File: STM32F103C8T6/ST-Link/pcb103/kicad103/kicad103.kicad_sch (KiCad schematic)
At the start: 32 parts, among them IC1 LD1117DT33TR, J1 0480372200, J2 Conn_01x02_Socket, J3 Conn_02x05_Odd_Even, J5 Conn_01x16_Pin, J7 Conn_01x04_Pin, J8 Conn_01x05_Socket, J9 Conn_01x17_Pin, U1 STM32F103C8T6, Y1 8MHz 20pF

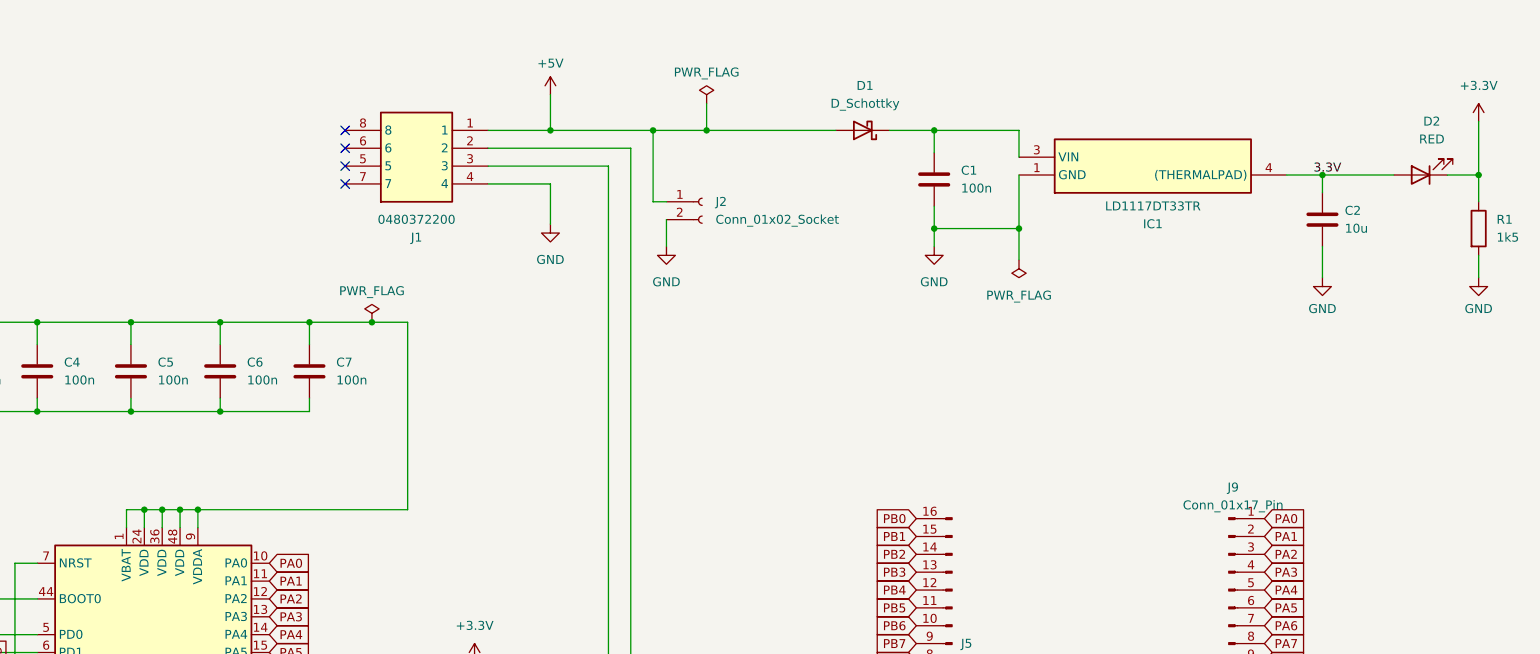
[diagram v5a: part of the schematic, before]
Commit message: Fix power lines
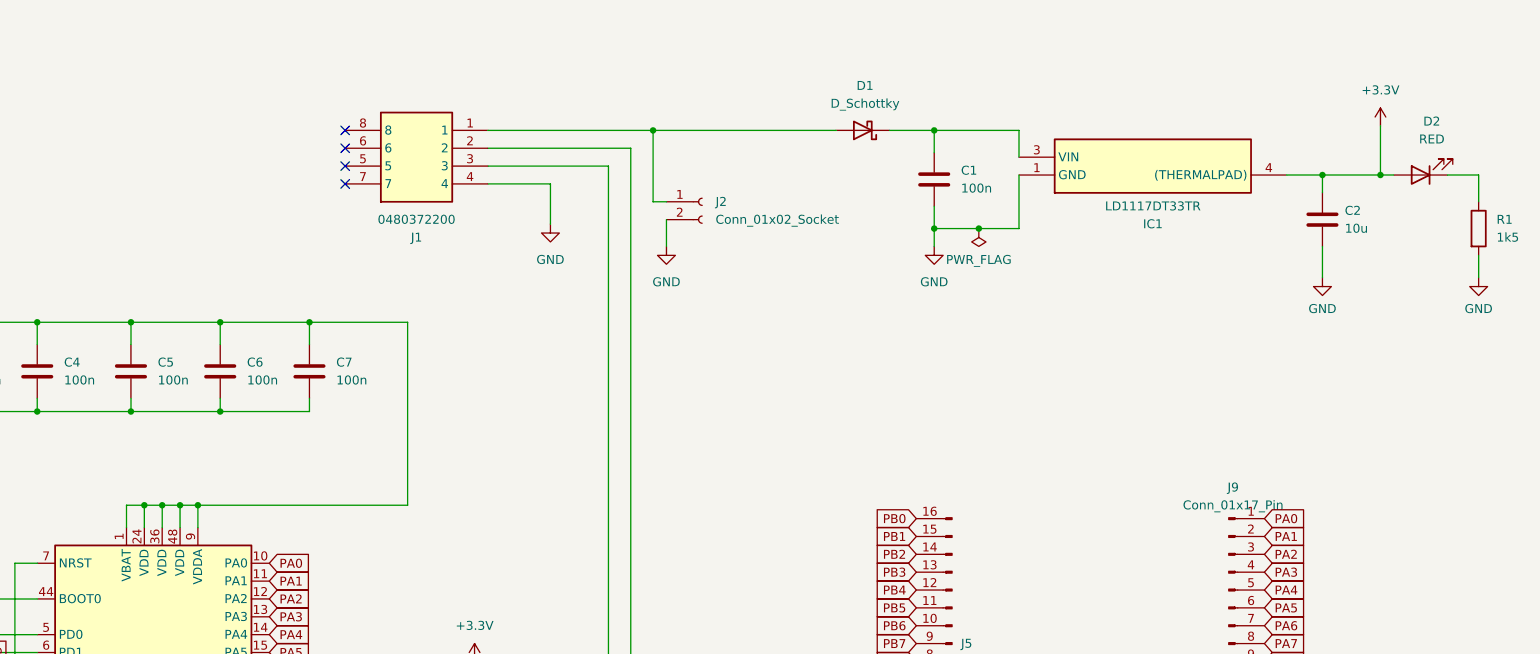
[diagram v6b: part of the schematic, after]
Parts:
- IC1: footprint Library:TO228P972X240-3N -> TO228P972X240-3N
- J1: footprint Library:0480372200 -> 0480372200
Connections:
- net 3.3V is gone; now on net +3.3V: C2.1, D2.2 (A), IC1.4 ((THERMALPAD))
- net +3.3V: no longer D2.1 (K), R1.1
- net +5V: no longer names the net of D1.2 (A), J1.1, J2.1 (Pin_1)
- new net: D2.1 (K), R1.1

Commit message: Connect Debug
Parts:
- IC1: footprint TO228P972X240-3N -> Library:TO228P972X240-3N
- J1: footprint 0480372200 -> Library:0480372200
- J7: footprint Connector_PinHeader_2.54mm:PinHeader_1x04_P2.54mm_Vertical -> Connector_PinSocket_2.54mm:PinSocket_1x04_P2.54mm_Vertical
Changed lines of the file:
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@@
       (effects (font (size 1.27 1.27)))
     )
-    (property "Footprint" "TO228P972X240-3N" (at 243.205 -59.995 0)
+    (property "Footprint" "Library:TO228P972X240-3N" (at 243.205 -59.995 0)
       (effects (font (size 1.27 1.27)) (justify left top) hide)
     )
@@
       (effects (font (size 1.27 1.27)))
     )
-    (property "Footprint" "Connector_PinHeader_2.54mm:PinHeader_1x04_P2.54mm_Vertical" (at 241.3 146.685 0)
+    (property "Footprint" "Connector_PinSocket_2.54mm:PinSocket_1x04_P2.54mm_Vertical" (at 241.3 146.685 0)
       (effects (font (size 1.27 1.27)) hide)
     )
@@
       (effects (font (size 1.27 1.27)))
     )
-    (property "Footprint" "0480372200" (at 129.54 -58.725 0)
+    (property "Footprint" "Library:0480372200" (at 129.54 -58.725 0)
       (effects (font (size 1.27 1.27)) (justify left top) hide)
     )

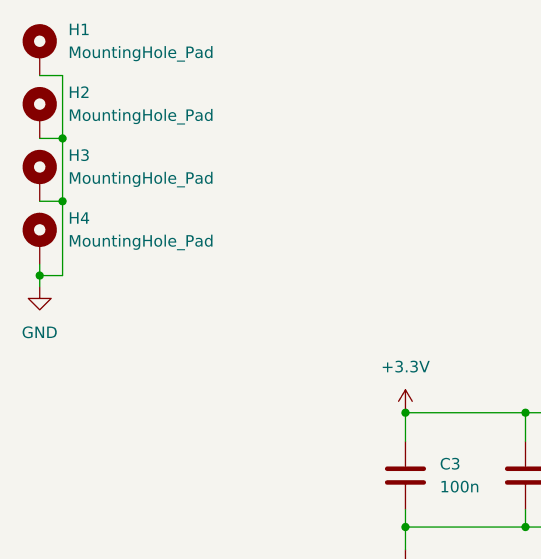
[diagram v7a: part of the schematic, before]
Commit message: Move out mounting hole
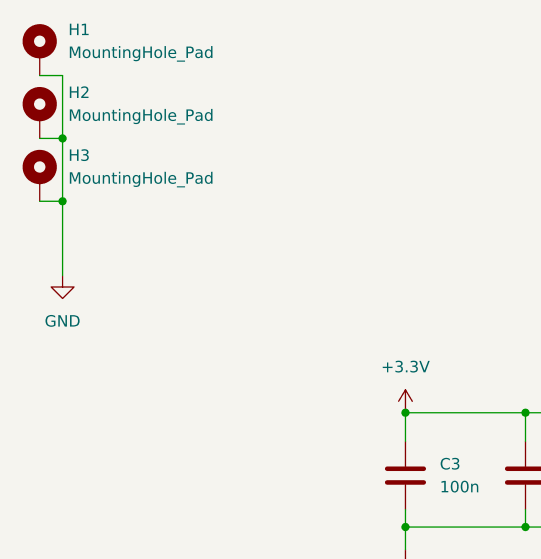
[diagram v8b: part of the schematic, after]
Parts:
- removed H4: MountingHole_Pad, MountingHole:MountingHole_4.3mm_M4_Pad_Via, symbol Mechanical:MountingHole_Pad
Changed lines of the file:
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@@
   (junction (at 156.845 28.575) (diameter 0) (color 0 0 0 0)
-  )
-  (junction (at 15.24 40.64) (diameter 0) (color 0 0 0 0)
   )
   (junction (at 196.85 42.545) (diameter 0) (color 0 0 0 0)
@@
     (stroke (width 0) (type default))
   )
-  (wire (pts (xy 15.24 39.37) (xy 15.24 40.64))
-    (stroke (width 0) (type default))
-  )
   (wire (pts (xy 156.845 28.575) (xy 156.845 38.735))
     (stroke (width 0) (type default))
@@
     (stroke (width 0) (type default))
   )
-  (wire (pts (xy 17.78 40.64) (xy 15.24 40.64))
-    (stroke (width 0) (type default))
-  )
   (wire (pts (xy 60.325 125.73) (xy 60.325 173.355))
     (stroke (width 0) (type default))
@@
   )
   (wire (pts (xy 274.32 46.355) (xy 274.32 49.53))
-    (stroke (width 0) (type default))
-  )
-  (wire (pts (xy 15.24 40.64) (xy 15.24 41.91))
     (stroke (width 0) (type default))
   )
@@
     )
   )
-  (symbol (lib_id "Mechanical:MountingHole_Pad") (at 15.24 36.83 0) (unit 1)
-    (in_bom yes) (on_board yes) (dnp no) (fields_autoplaced)
-    (property "Reference" "H4" (at 18.415 34.29 0)
-      (effects (font (size 1.27 1.27)) (justify left))
-    )
-    (property "Value" "MountingHole_Pad" (at 18.415 36.83 0)
-      (effects (font (size 1.27 1.27)) (justify left))
-    )
-    (property "Footprint" "MountingHole:MountingHole_4.3mm_M4_Pad_Via" (at 15.24 36.83 0)
-      (effects (font (size 1.27 1.27)) hide)
-    )
-    (property "Datasheet" "~" (at 15.24 36.83 0)
-      (effects (font (size 1.27 1.27)) hide)
-    )
-    (pin "1")
-    (instances
-      (project "kicad103"
-        (path "/185c057b-9149-49f2-8708-a9b3e40a18db"
-          (reference "H4") (unit 1)
-        )
-      )
-    )
-  )
   (symbol (lib_id "Connector:Conn_01x02_Socket") (at 163.83 38.735 0) (unit 1)
     (in_bom yes) (on_board yes) (dnp no) (fields_autoplaced)
@@
     )
   )
-  (symbol (lib_id "power:GND") (at 15.24 41.91 0) (unit 1)
-    (in_bom yes) (on_board yes) (dnp no) (fields_autoplaced)
-    (property "Reference" "#PWR022" (at 15.24 48.26 0)
-      (effects (font (size 1.27 1.27)) hide)
-    )
-    (property "Value" "GND" (at 15.24 46.99 0)
-      (effects (font (size 1.27 1.27)))
-    )
-    (property "Footprint" "" (at 15.24 41.91 0)
-      (effects (font (size 1.27 1.27)) hide)
-    )
-    (property "Datasheet" "" (at 15.24 41.91 0)
-      (effects (font (size 1.27 1.27)) hide)
-    )
+  (symbol (lib_id "power:GND") (at 17.78 40.64 0) (unit 1)
+    (in_bom yes) (on_board yes) (dnp no) (fields_autoplaced)
+    (property "Reference" "#PWR022" (at 17.78 46.99 0)
+      (effects (font (size 1.27 1.27)) hide)
+    )
+    (property "Value" "GND" (at 17.78 45.72 0)
+      (effects (font (size 1.27 1.27)))
+    )
+    (property "Footprint" "" (at 17.78 40.64 0)
+      (effects (font (size 1.27 1.27)) hide)
+    )
+    (property "Datasheet" "" (at 17.78 40.64 0)
+      (effects (font (size 1.27 1.27)) hide)
+    )
